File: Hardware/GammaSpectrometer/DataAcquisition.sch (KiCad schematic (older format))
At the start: 2 parts, among them U2 PIC32MZ0512EFE064, U3 MCP33131-10

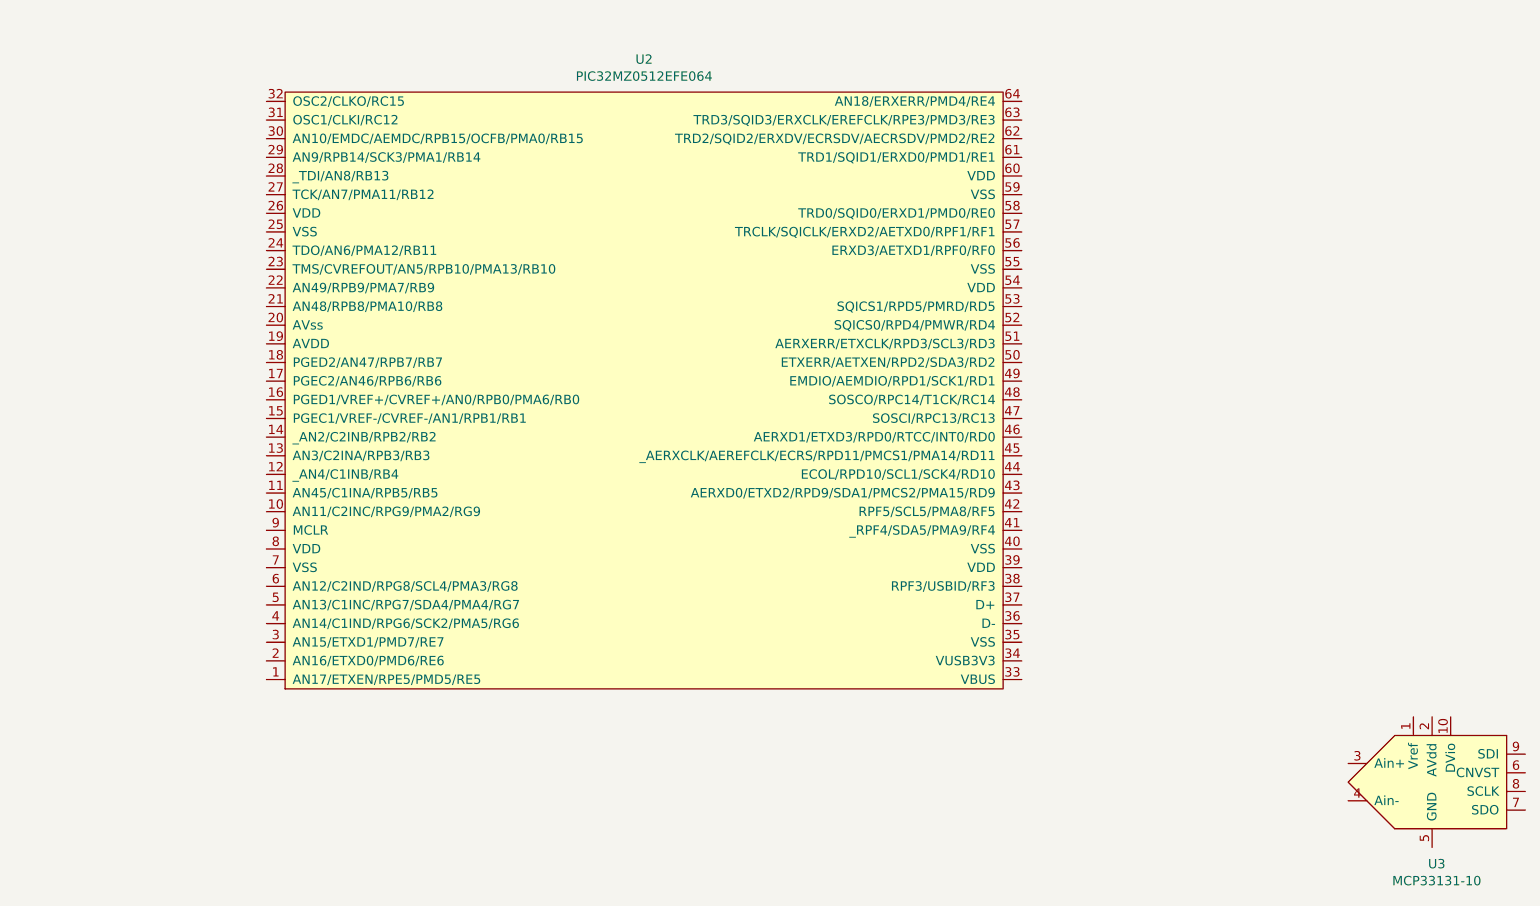
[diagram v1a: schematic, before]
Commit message: draft of component placement on PCB
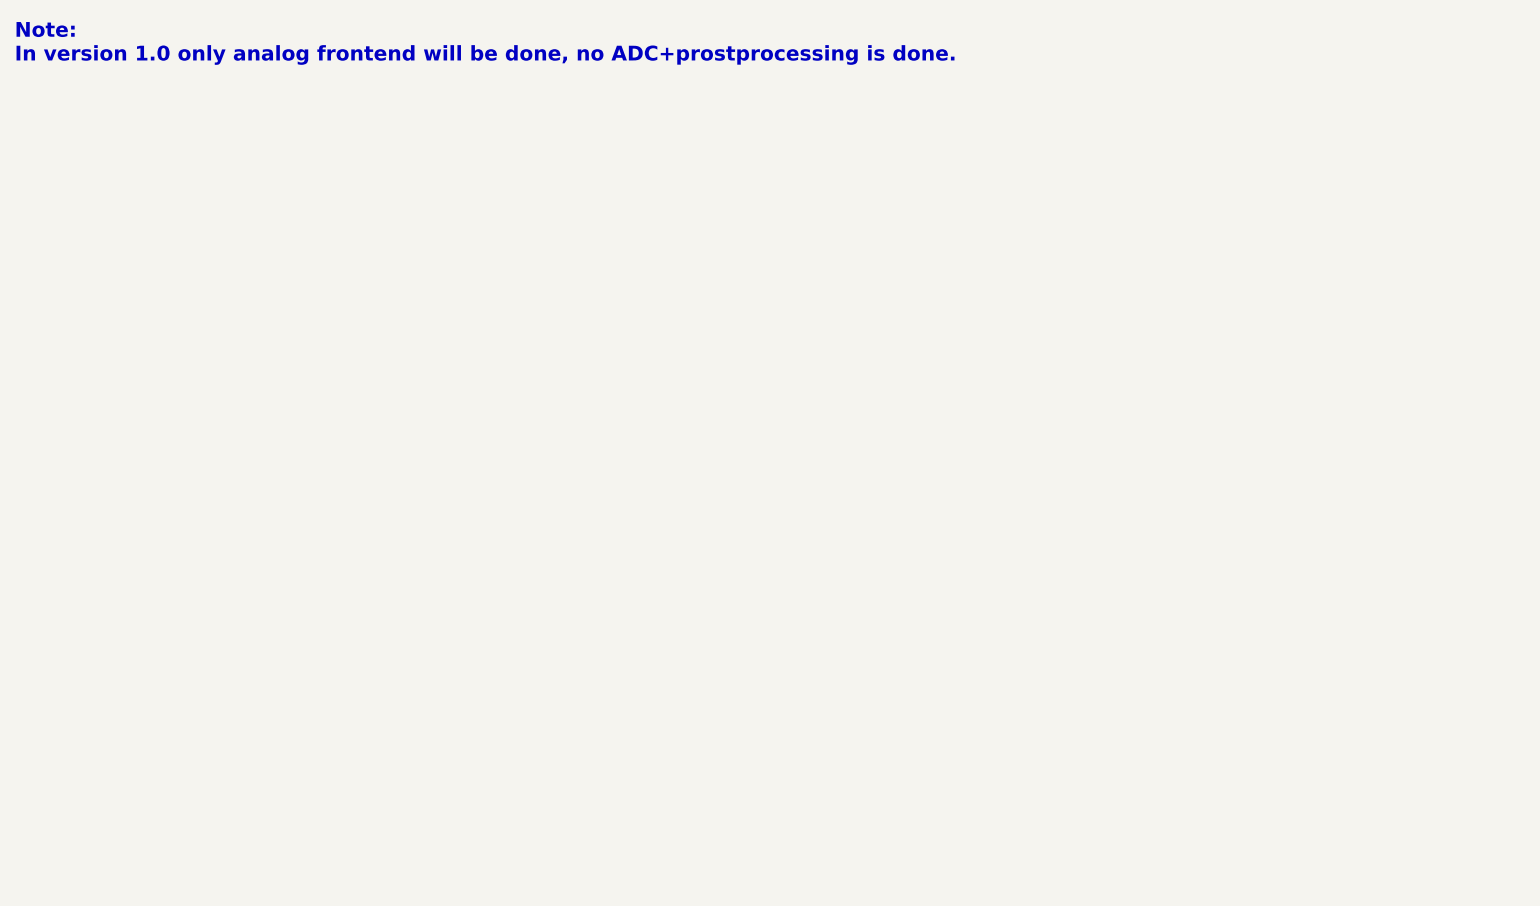
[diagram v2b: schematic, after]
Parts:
- removed U2: PIC32MZ0512EFE064, Package_QFP:LQFP-64-1EP_10x10mm_P0.5mm_EP6.5x6.5mm, symbol GammaSpectrometer:PIC32MZ0512EFE064
- removed U3: MCP33131-10, Package_SO:MSOP-10_3x3mm_P0.5mm, symbol GammaSpectrometer:MCP33131-10
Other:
- note added: "Note:\nIn version 1.0 only analog frontend will be done, no ADC+prostprocessing is done."
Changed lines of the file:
@@
 Comment4 ""
 $EndDescr
-$Comp
-L GammaSpectrometer:PIC32MZ0512EFE064 U2
-U 1 1 5FBBA8A7
-P 4500 1450
-F 0 "U2" H 4425 1625 50  0000 C CNN
-F 1 "PIC32MZ0512EFE064" H 4425 1534 50  0000 C CNN
-F 2 "Package_QFP:LQFP-64-1EP_10x10mm_P0.5mm_EP6.5x6.5mm" H 4500 1500 50  0001 C CNN
-F 3 "" H 4500 1500 50  0001 C CNN
-	1    4500 1450
-	1    0    0    -1
-$EndComp
-$Comp
-L GammaSpectrometer:MCP33131-10 U3
-U 1 1 5FBBB2A7
-P 8650 5150
-F 0 "U3" H 8675 4711 50  0000 C CNN
-F 1 "MCP33131-10" H 8675 4620 50  0000 C CNN
-F 2 "Package_SO:MSOP-10_3x3mm_P0.5mm" H 9050 5450 50  0001 C CNN
-F 3 "" H 9050 5450 50  0001 C CNN
-	1    8650 5150
-	1    0    0    -1
-$EndComp
+Text Notes 1050 1300 0    79   ~ 16
+Note:\nIn version 1.0 only analog frontend will be done, no ADC+prostprocessing is done.
 $EndSCHEMATC
